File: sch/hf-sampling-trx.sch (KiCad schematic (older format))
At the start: 2 parts

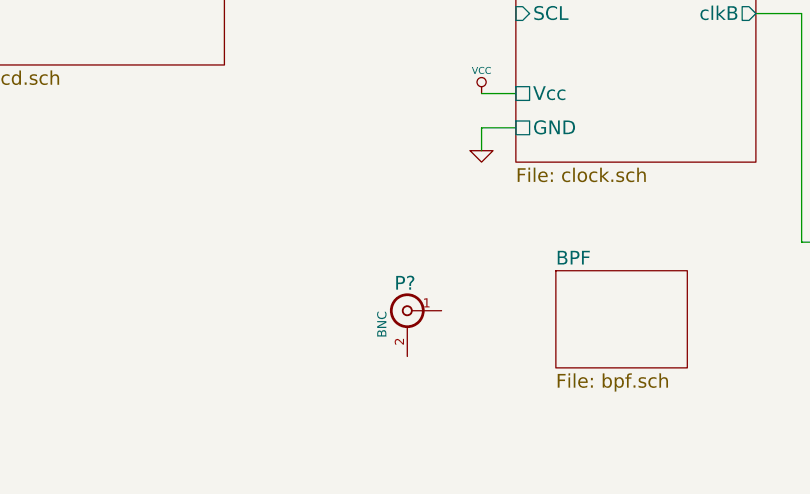
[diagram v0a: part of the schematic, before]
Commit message: add FIN1002 buffer for LVDS variant of Si570
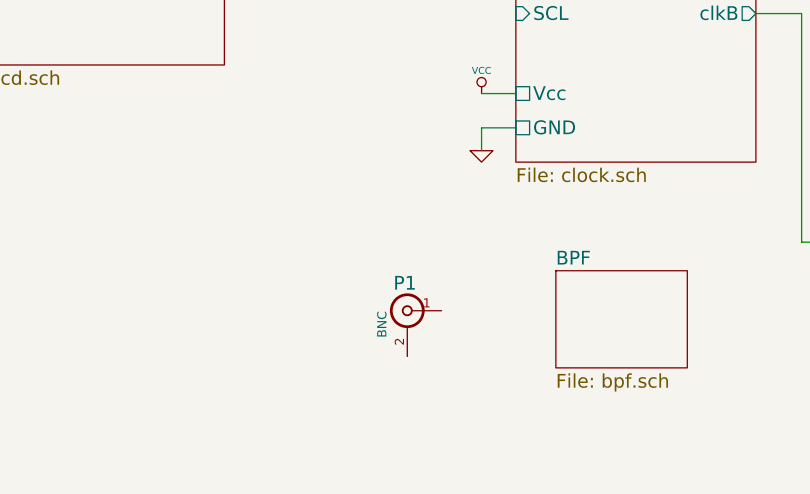
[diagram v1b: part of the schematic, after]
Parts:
- gave numbers to parts that had none: 1
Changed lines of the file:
@@
-EESchema Schematic File Version 2  date so 30 črv 00:27:21 2012
+EESchema Schematic File Version 2  date so 30 črv 11:50:59 2012
 LIBS:power
 LIBS:device
@@
 LIBS:ms-audio
 LIBS:ms-conn
+LIBS:ms-ti
+LIBS:hf-sampling-trx-cache
 EELAYER 25  0
 EELAYER END
 $Descr A4 11693 8268
 encoding utf-8
-Sheet 1 4
+Sheet 1 5
 Title ""
-Date "29 jun 2012"
+Date "30 jun 2012"
 Rev ""
 Comp ""
@@
 	7825 3575 9075 3575
 $Comp
-L BNC P?
+L BNC P1
 U 1 1 4FEE47FB
 P 3725 3500
-F 0 "P?" H 3735 3620 60  0000 C CNN
+F 0 "P1" H 3735 3620 60  0000 C CNN
 F 1 "BNC" V 3835 3440 40  0000 C CNN
 	1    3725 3500
